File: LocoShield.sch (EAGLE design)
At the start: 15 parts, among them J2 RJ12, J3 RJ12, Q1 2N3904, U1 LM393N

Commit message: 0.1
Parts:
- LED1: device MCP:LEDB155 -> led:LEDB156
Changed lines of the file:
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@@
 <layers>
 <layer number="1" name="Top" color="4" fill="1" visible="no" active="no"/>
+<layer number="2" name="Route2" color="1" fill="3" visible="no" active="no"/>
+<layer number="3" name="Route3" color="4" fill="3" visible="no" active="no"/>
+<layer number="14" name="Route14" color="1" fill="6" visible="no" active="no"/>
+<layer number="15" name="Route15" color="4" fill="6" visible="no" active="no"/>
 <layer number="16" name="Bottom" color="2" fill="1" visible="no" active="no"/>
 <layer number="17" name="Pads" color="6" fill="1" visible="no" active="no"/>
@@
 <part name="U1" library="MCP" deviceset="LM393" device="N"/>
 <part name="R9" library="rcl" deviceset="R-US_" device="0204/5" value="47R"/>
-<part name="LED1" library="MCP" deviceset="LED" device="B155"/>
+<part name="LED1" library="led" deviceset="LED" device="B156"/>
 <part name="J1" library="con-lstb" deviceset="MA04-1" device=""/>
 <part name="P+1" library="supply1" deviceset="VCC" device=""/>

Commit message: 1.0
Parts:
- added U2: ARDUINO_SHIELDNOHOLES, SparkFun:ARDUINO_SHIELDNOHOLES
- LED1: device led:LEDB156 -> led:LEDB155
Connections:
- net GND: now also U2.GND@0, U2.GND@1, U2.GND@2
- net LNRX: now also U2.D8
- net LNTX: now also U2.D7
- net VCC: now also U2.5V
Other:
- note added: "Loconet Shield"
- note removed: "Loconet Protoboard"
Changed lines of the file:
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@@
 <layer number="18" name="Vias" color="2" fill="1" visible="no" active="no"/>
 <layer number="19" name="Unrouted" color="21" fill="1" visible="no" active="no"/>
-<layer number="20" name="Dimension" color="24" fill="1" visible="no" active="no"/>
+<layer number="20" name="Dimension" color="27" fill="1" visible="no" active="no"/>
 <layer number="21" name="tPlace" color="3" fill="1" visible="no" active="no"/>
 <layer number="22" name="bPlace" color="14" fill="1" visible="no" active="no"/>
@@
 <layer number="49" name="Reference" color="12" fill="1" visible="no" active="no"/>
 <layer number="50" name="dxf" color="7" fill="1" visible="no" active="no"/>
-<layer number="51" name="tDocu" color="6" fill="1" visible="no" active="no"/>
+<layer number="51" name="tDocu" color="61" fill="1" visible="no" active="no"/>
 <layer number="52" name="bDocu" color="7" fill="1" visible="no" active="no"/>
 <layer number="53" name="tGND_GNDA" color="7" fill="9" visible="no" active="no"/>
@@
 <layer number="121" name="_tsilk" color="7" fill="1" visible="yes" active="yes"/>
 <layer number="122" name="_bsilk" color="7" fill="1" visible="yes" active="yes"/>
+<layer number="125" name="_tNames" color="7" fill="1" visible="no" active="yes"/>
+<layer number="144" name="Drill_legend" color="7" fill="1" visible="no" active="yes"/>
 <layer number="151" name="HeatSink" color="7" fill="1" visible="yes" active="yes"/>
 <layer number="199" name="Contour" color="7" fill="1" visible="yes" active="yes"/>
@@
 <layer number="207" name="207bmp" color="8" fill="10" visible="yes" active="yes"/>
 <layer number="208" name="208bmp" color="9" fill="10" visible="yes" active="yes"/>
+<layer number="209" name="209bmp" color="7" fill="1" visible="no" active="yes"/>
+<layer number="210" name="210bmp" color="7" fill="1" visible="no" active="yes"/>
+<layer number="211" name="211bmp" color="7" fill="1" visible="no" active="yes"/>
+<layer number="212" name="212bmp" color="7" fill="1" visible="no" active="yes"/>
+<layer number="213" name="213bmp" color="7" fill="1" visible="no" active="yes"/>
+<layer number="214" name="214bmp" color="7" fill="1" visible="no" active="yes"/>
+<layer number="215" name="215bmp" color="7" fill="1" visible="no" active="yes"/>
+<layer number="216" name="216bmp" color="7" fill="1" visible="no" active="yes"/>
+<layer number="217" name="217bmp" color="18" fill="1" visible="no" active="no"/>
+<layer number="218" name="218bmp" color="19" fill="1" visible="no" active="no"/>
+<layer number="219" name="219bmp" color="20" fill="1" visible="no" active="no"/>
+<layer number="220" name="220bmp" color="21" fill="1" visible="no" active="no"/>
+<layer number="221" name="221bmp" color="22" fill="1" visible="no" active="no"/>
+<layer number="222" name="222bmp" color="23" fill="1" visible="no" active="no"/>
+<layer number="223" name="223bmp" color="24" fill="1" visible="no" active="no"/>
+<layer number="224" name="224bmp" color="25" fill="1" visible="no" active="no"/>
 <layer number="250" name="Descript" color="3" fill="1" visible="yes" active="yes"/>
 <layer number="251" name="SMDround" color="12" fill="11" visible="yes" active="yes"/>
@@
 <part name="U1" library="MCP" deviceset="LM393" device="N"/>
 <part name="R9" library="rcl" deviceset="R-US_" device="0204/5" value="47R"/>
-<part name="LED1" library="led" deviceset="LED" device="B156"/>
+<part name="LED1" library="led" deviceset="LED" device="B155"/>
 <part name="J1" library="con-lstb" deviceset="MA04-1" device=""/>
 <part name="P+1" library="supply1" deviceset="VCC" device=""/>
 <part name="V3" library="supply2" deviceset="GND" device=""/>
+<part name="U2" library="SparkFun" deviceset="ARDUINO_SHIELD" device="NOHOLES"/>
+<part name="P+2" library="supply1" deviceset="VCC" device=""/>
+<part name="V4" library="supply2" deviceset="GND" device=""/>
 </parts>
 <sheets>
@@
 <wire x1="70.612" y1="62.23" x2="70.612" y2="137.16" width="0.1524" layer="250"/>
 <text x="105.41" y="68.58" size="2.54" layer="250">Loconet Interface</text>
-<text x="154.94" y="27.94" size="5.08" layer="250">Loconet Protoboard</text>
+<text x="154.94" y="27.94" size="5.08" layer="250">Loconet Shield</text>
 <text x="238.76" y="7.62" size="2.54" layer="250">1.0</text>
 <text x="195.58" y="96.52" size="1.778" layer="92">D7</text>
@@
 <instance part="P+1" gate="VCC" x="185.42" y="104.14"/>
 <instance part="V3" gate="GND" x="185.42" y="91.44"/>
+<instance part="U2" gate="G$1" x="205.74" y="152.4"/>
+<instance part="P+2" gate="VCC" x="187.96" y="149.86"/>
+<instance part="V4" gate="GND" x="187.96" y="132.08"/>
 </instances>
 <busses>
@@
 <pinref part="V3" gate="GND" pin="GND"/>
 </segment>
+<segment>
+<wire x1="193.04" y1="139.7" x2="193.04" y2="137.16" width="0.1524" layer="91"/>
+<wire x1="193.04" y1="137.16" x2="193.04" y2="134.62" width="0.1524" layer="91"/>
+<wire x1="193.04" y1="134.62" x2="187.96" y2="134.62" width="0.1524" layer="91"/>
+<junction x="193.04" y="137.16"/>
+<junction x="193.04" y="134.62"/>
+<pinref part="U2" gate="G$1" pin="GND@2"/>
+<pinref part="U2" gate="G$1" pin="GND@1"/>
+<pinref part="U2" gate="G$1" pin="GND@0"/>
+<pinref part="V4" gate="GND" pin="GND"/>
+</segment>
 </net>
 <net name="DCCRAILSYNC-" class="0">
@@
 <pinref part="J1" gate="1" pin="1"/>
 <pinref part="P+1" gate="VCC" pin="VCC"/>
+</segment>
+<segment>
+<wire x1="193.04" y1="147.32" x2="187.96" y2="147.32" width="0.1524" layer="91"/>
+<pinref part="U2" gate="G$1" pin="5V"/>
+<pinref part="P+2" gate="VCC" pin="VCC"/>
 </segment>
 </net>
@@
 <pinref part="R1" gate="G$1" pin="1"/>
 </segment>
+<segment>
+<wire x1="218.44" y1="149.86" x2="223.52" y2="149.86" width="0.1524" layer="91"/>
+<label x="223.52" y="149.86" size="1.016" layer="95" xref="yes"/>
+<pinref part="U2" gate="G$1" pin="D7"/>
+</segment>
 </net>
 <net name="LNRX" class="0">
@@
 <pinref part="LED1" gate="G$1" pin="C"/>
 </segment>
-</net>
+<segment>
+<wire x1="218.44" y1="147.32" x2="223.52" y2="147.32" width="0.1524" layer="91"/>
+<label x="223.52" y="147.32" size="1.016" layer="95" xref="yes"/>
+<pinref part="U2" gate="G$1" pin="D8"/>
+</segment>
+</net>

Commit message: 1.1
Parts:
- removed J1: (no value), con-lstb:MA04-1
- added JP1, JP2, JP5, JP6: (no value), MCP:JUMPER-2PTH_LOCK
- added JP3: LN-TERM, MCP:JUMPER-2PTH_LOCK
- added JP4: (no value), MCP:M05LOCK
- added R10: 82R, rcl:R-US_0204/5
- added SHIELD: ARDUINO_SHIELDNOHOLES, SparkFun:ARDUINO_SHIELDNOHOLES
- U1: value LM393N -> LM393; device MCP:LM393N -> MCP:LM393
- U2: value ARDUINO_SHIELDNOHOLES -> LM317LZ; device SparkFun:ARDUINO_SHIELDNOHOLES -> linear:LM317LZ
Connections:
- new net N$10: JP6.1, SHIELD.D4
- new net N$3: JP1.1, SHIELD.D7
- new net N$4: JP2.1, SHIELD.D8
- new net N$7: R10.1, U2.VO
- new net N$8: JP3.2, R10.2, U2.ADJ
- new net N$9: JP5.1, SHIELD.*D5
- new net V+: JP4.1, SHIELD.VIN, U2.VI
- net GND: now also JP4.5, SHIELD.GND@0, SHIELD.GND@1, SHIELD.GND@2; no longer J1.4, U2.GND@0, U2.GND@1, U2.GND@2
- net LNRX: now also JP2.2, JP4.3, JP6.2; no longer J1.2, U2.D8
- net LNTX: now also JP1.2, JP4.4, JP5.2; no longer J1.3, U2.D7
- net LOCONET: now also JP3.1
- net VCC: now also JP4.2, SHIELD.5V; no longer J1.1, U2.5V
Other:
- note added: "1.1C"
- note added: "LocoShield"
- note removed: "1.0"
- note removed: "Loconet Shield"

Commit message: 1.2
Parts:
- removed JP3: LN-TERM, MCP:JUMPER-2PTH_LOCK
- removed JP4: (no value), MCP:M05LOCK
- removed JP5, JP6: (no value), MCP:JUMPER-2PTH_LOCK
- removed R10: 82R, rcl:R-US_0204/5
- removed SHIELD: ARDUINO_SHIELDNOHOLES, SparkFun:ARDUINO_SHIELDNOHOLES
- added J1: (no value), con-lstb:MA04-1
- LED1: device led:LEDB155 -> MCP:LEDCHIPLED_0805
- Q1: device transistor:2N3904 -> MCP:NPN-SOT23-3
- R1: value 4k7 -> 470R; device rcl:R-US_0204/5 -> rcl:R-US_R0805W
- R2: value 27k -> 1k; device rcl:R-US_0204/5 -> rcl:R-US_R0805W
- R3: value 39k -> 27k; device rcl:R-US_0204/5 -> rcl:R-US_R0805W
- R4: value 47k -> 39k; device rcl:R-US_0204/5 -> rcl:R-US_R0805W
- R5: value 150k -> 240k; device rcl:R-US_0204/5 -> rcl:R-US_R0805W
- R6: value 240k -> 150k; device rcl:R-US_0204/5 -> rcl:R-US_R0805W
- R7: value 1k -> 47k; device rcl:R-US_0204/5 -> rcl:R-US_R0805W
- R8: value 470R -> 47R; device rcl:R-US_0204/5 -> rcl:R-US_R0805W
- R9: value 47R -> 4k7; device rcl:R-US_0204/5 -> rcl:R-US_R0805W
- U1: value LM393 -> LM393M; device MCP:LM393 -> MCP:LM393M
- U2: value LM317LZ -> ARDUINO_SHIELDNOHOLES; device linear:LM317LZ -> SparkFun:ARDUINO_SHIELDNOHOLES
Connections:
- removed net N$10: JP6.1, SHIELD.D4
- removed net N$7: R10.1, U2.VO
- removed net N$8: JP3.2, R10.2, U2.ADJ
- removed net N$9: JP5.1, SHIELD.*D5
- removed net V+: JP4.1, SHIELD.VIN, U2.VI
- net GND: now also J1.4, R4.1, R6.1, R8.1, U2.GND@0, U2.GND@1, U2.GND@2; no longer JP4.5, R3.1, R5.1, R9.1, SHIELD.GND@0, SHIELD.GND@1, SHIELD.GND@2
- net LNRX: now also J1.2, R2.2, R5.2; no longer JP4.3, JP6.2, R6.2, R7.2
- net LNTX: now also J1.3, R9.1; no longer JP4.4, JP5.2, R1.1
- net LOCONET: now also R7.1; no longer JP3.1, R4.1
- net N$1: now also R9.2; no longer R1.2
- net N$15: now also R1.2; no longer R8.2
- net N$2: now also R5.1, R6.2, R7.2; no longer R4.2, R5.2, R6.1
- net N$3: now also U2.D7; no longer SHIELD.D7
- net N$4: now also U2.D8; no longer SHIELD.D8
- net N$5: now also R4.2; no longer R2.2
- net N$6: now also R8.2; no longer R9.2
- net VCC: now also J1.1, R1.1, R3.1, U2.5V; no longer JP4.2, R7.1, R8.1, SHIELD.5V
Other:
- note added: "1.2"
- note added: "Loconet Shield"
- note removed: "1.1C"
- note removed: "LocoShield"
- moved on the sheet: R1, R2, R3, R4, R5, R6, R7, R8, R9

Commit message: 1.3
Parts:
- removed J1: (no value), con-lstb:MA04-1
- added JP3: LN-TERM, MCP:JUMPER-2PTH_LOCK
- added R10: 82R, rcl:R-US_R0805
- added SHIELD: ARDUINO_SHIELDNOHOLES, SparkFun:ARDUINO_SHIELDNOHOLES
- added SV1: (no value), con-lstb:MA05-1
- U2: value ARDUINO_SHIELDNOHOLES -> LM317LCDR; device SparkFun:ARDUINO_SHIELDNOHOLES -> MCP:LM317LD
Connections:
- new net N$20: JP3.2, R10.2, U2.ADJ
- new net V+: SHIELD.VIN, SV1.1, U2.VI
- new net VOUT: R10.1, U2.VO, U2.VO@1, U2.VO@2, U2.VO@3
- net GND: now also SHIELD.GND@0, SHIELD.GND@1, SHIELD.GND@2, SV1.5; no longer J1.4, U2.GND@0, U2.GND@1, U2.GND@2
- net LNRX: now also SV1.3; no longer J1.2
- net LNTX: now also SV1.4; no longer J1.3
- net LOCONET: now also JP3.1
- net N$3: now also SHIELD.D7; no longer U2.D7
- net N$4: now also SHIELD.D8; no longer U2.D8
- net VCC: now also SHIELD.5V, SV1.2; no longer J1.1, U2.5V
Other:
- note added: "1.3"
- note removed: "1.2"

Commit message: 1.4
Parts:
- removed JP1, JP2: (no value), MCP:JUMPER-2PTH_LOCK
- added JPD10, JPD11, JPD4, JPD5, JPD6, JPD7, JPD8, JPD9: (no value), MCP:JP2E
- LED1: value (none) -> Blue; device MCP:LEDCHIPLED_0805 -> SPCoast:LED0805-LED
- R1, R2, R3, R4, R5, R6, R7, R8, R9: device rcl:R-US_R0805W -> SPCoast:R0805-RES
- R10: device rcl:R-US_R0805 -> SPCoast:R0805-RES
- SHIELD: value ARDUINO_SHIELDNOHOLES -> ARDUINO_SHIELDNO_SILK; device SparkFun:ARDUINO_SHIELDNOHOLES -> SPCoast:ARDUINO_SHIELDNO_SILK
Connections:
- removed net N$3: JP1.1, SHIELD.D7
- removed net N$4: JP2.1, SHIELD.D8
- new net D10: JPD10.2, SHIELD.*D10
- new net D11: JPD11.2, SHIELD.*D11
- new net D4: JPD4.2, SHIELD.D4
- new net D5: JPD5.2, SHIELD.*D5
- new net D6: JPD6.2, SHIELD.*D6
- new net D7: JPD7.2, SHIELD.D7
- new net D8: JPD8.2, SHIELD.D8
- new net D9: JPD9.2, SHIELD.*D9
- net GND: now also R8.2; no longer R8.1
- net LNRX: now also JPD10.1, JPD11.1, JPD4.1, JPD5.1, JPD6.1, JPD7.1, JPD8.1, JPD9.1; no longer JP2.2
- net LNTX: now also JPD10.3, JPD11.3, JPD4.3, JPD5.3, JPD6.3, JPD7.3, JPD8.3, JPD9.3; no longer JP1.2
- net N$6: now also R8.1; no longer R8.2
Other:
- note added: "1.4"
- note added: "Added D4-D11 RX/TX selection jumpers"
- note removed: "1.3"
- moved on the sheet: J2, J3, JP3, Q1, SV1, U1G1, U1G2, U2

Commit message: added missing values
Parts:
- J2, J3: value RJ12 -> RJ12/6
- JPD10, JPD11, JPD4, JPD5, JPD6, JPD7, JPD8, JPD9, SV1: value (none) -> 0.100
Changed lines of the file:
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@@
 </classes>
 <parts>
-<part name="J2" library="con-amp" deviceset="520250-3" device="" value="RJ12"/>
-<part name="J3" library="con-amp" deviceset="520250-3" device="" value="RJ12"/>
+<part name="J2" library="con-amp" deviceset="520250-3" device="" value="RJ12/6"/>
+<part name="J3" library="con-amp" deviceset="520250-3" device="" value="RJ12/6"/>
 <part name="V1" library="supply2" deviceset="GND" device=""/>
 <part name="R9" library="SPCoast" deviceset="R*" device="0805-RES" value="4k7"/>
@@
 <part name="U2" library="MCP" deviceset="LM317LD" device="" value="LM317LCDR"/>
 <part name="P+3" library="supply1" deviceset="V+" device=""/>
-<part name="SV1" library="con-lstb" deviceset="MA05-1" device=""/>
+<part name="SV1" library="con-lstb" deviceset="MA05-1" device="" value="0.100"/>
 <part name="P+4" library="supply1" deviceset="V+" device=""/>
-<part name="JPD7" library="MCP" deviceset="JP2E" device=""/>
-<part name="JPD6" library="MCP" deviceset="JP2E" device=""/>
-<part name="JPD5" library="MCP" deviceset="JP2E" device=""/>
-<part name="JPD4" library="MCP" deviceset="JP2E" device=""/>
-<part name="JPD8" library="MCP" deviceset="JP2E" device=""/>
-<part name="JPD9" library="MCP" deviceset="JP2E" device=""/>
-<part name="JPD10" library="MCP" deviceset="JP2E" device=""/>
-<part name="JPD11" library="MCP" deviceset="JP2E" device=""/>
+<part name="JPD7" library="MCP" deviceset="JP2E" device="" value="0.100"/>
+<part name="JPD6" library="MCP" deviceset="JP2E" device="" value="0.100"/>
+<part name="JPD5" library="MCP" deviceset="JP2E" device="" value="0.100"/>
+<part name="JPD4" library="MCP" deviceset="JP2E" device="" value="0.100"/>
+<part name="JPD8" library="MCP" deviceset="JP2E" device="" value="0.100"/>
+<part name="JPD9" library="MCP" deviceset="JP2E" device="" value="0.100"/>
+<part name="JPD10" library="MCP" deviceset="JP2E" device="" value="0.100"/>
+<part name="JPD11" library="MCP" deviceset="JP2E" device="" value="0.100"/>
 </parts>
 <sheets>

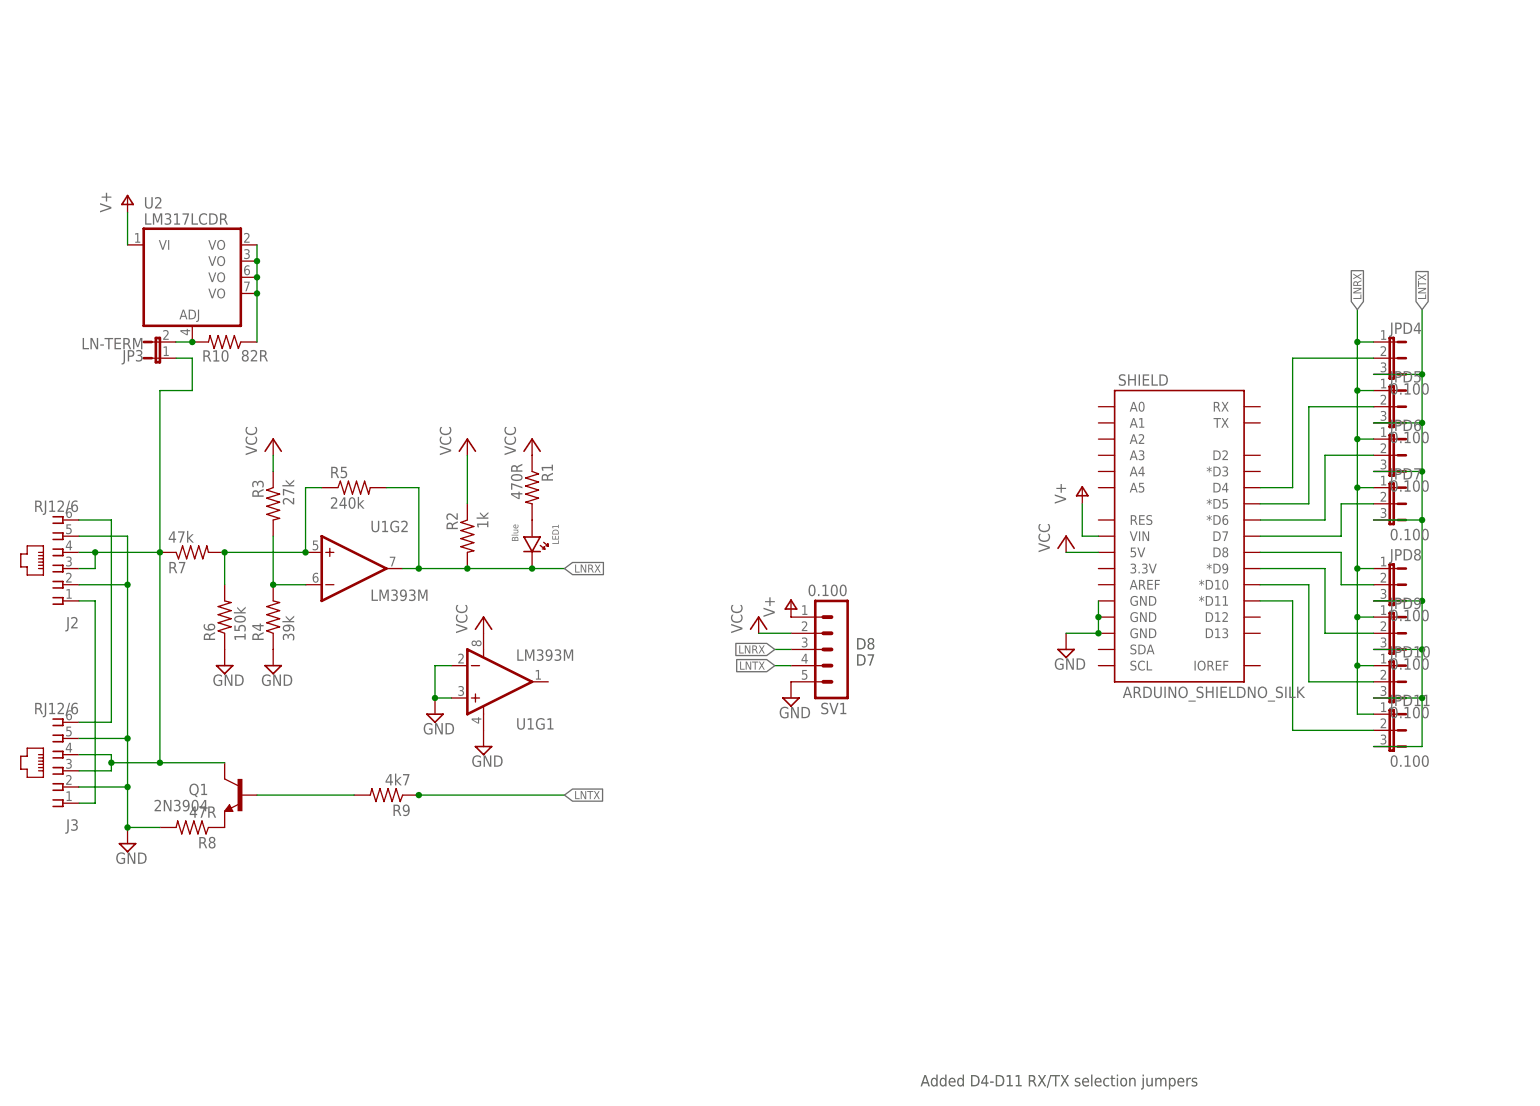
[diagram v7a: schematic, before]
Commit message: normalized values
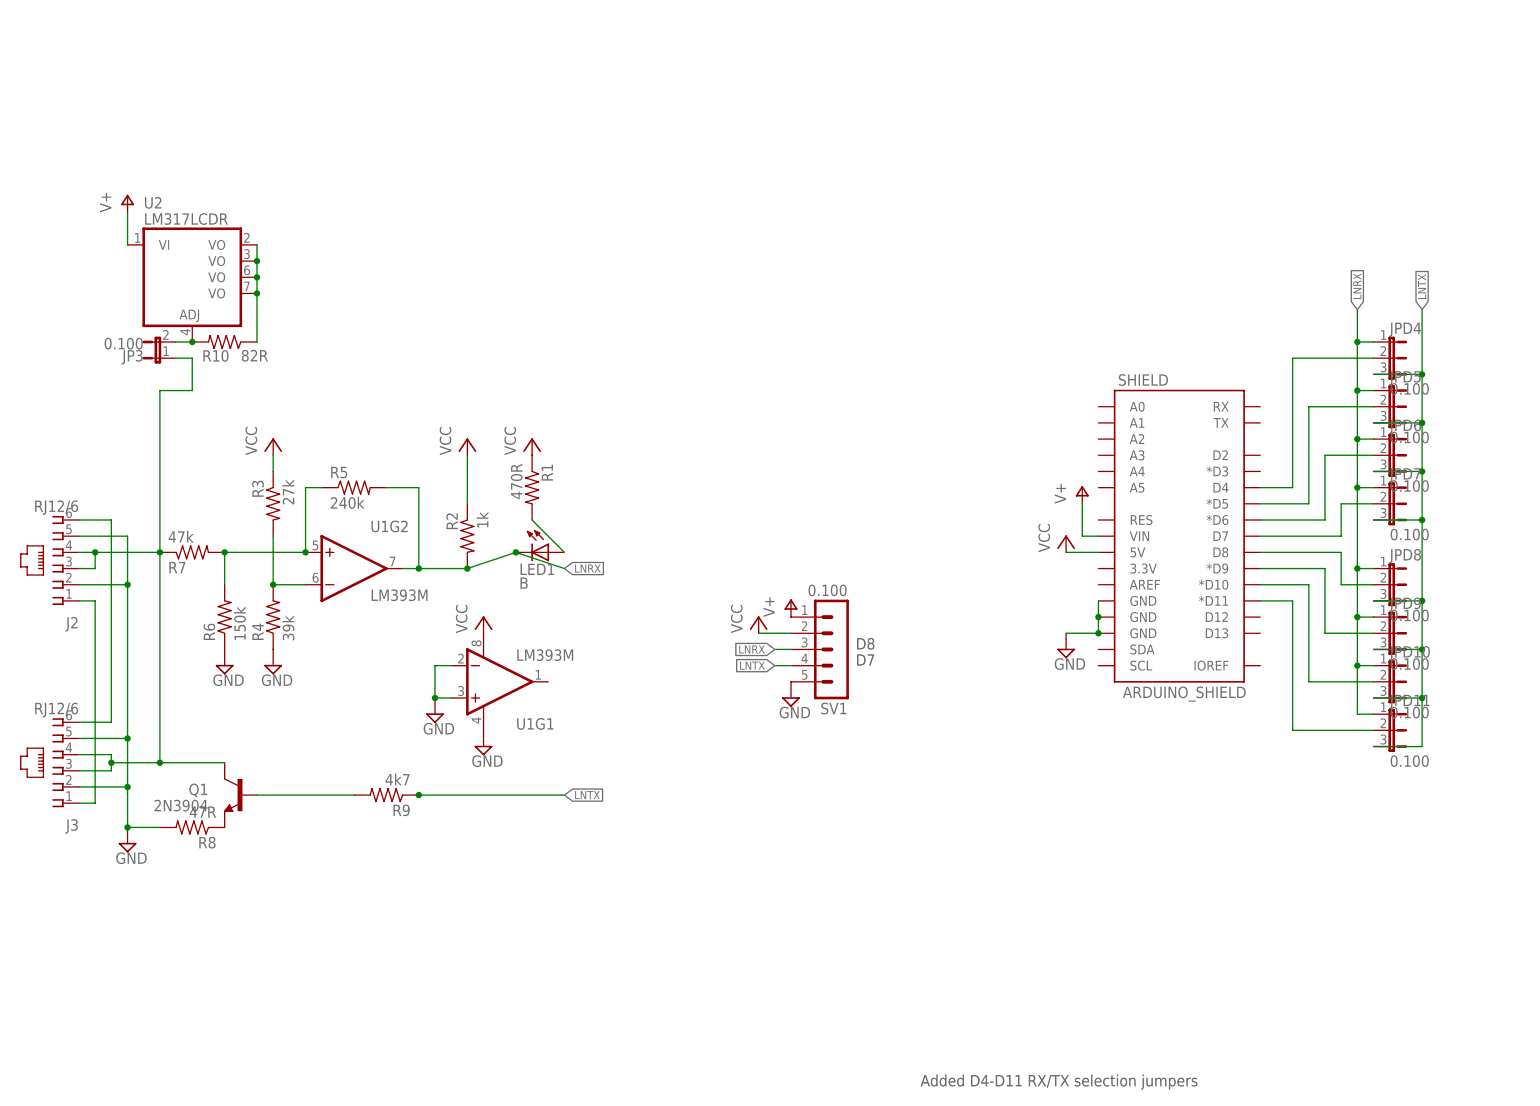
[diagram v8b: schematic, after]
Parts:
- J2, J3: device con-amp:520250-3 -> SPCoast:CONNECTOR-RJ25-6P6C
- JP3: value LN-TERM -> 0.100
- LED1: value Blue -> B; device SPCoast:LED0805-LED -> SPCoast:LED0603-LED
- R1, R2, R3, R4, R5, R6, R7, R8, R9: device SPCoast:R0805-RES -> SPCoast:R0603-RES
- SHIELD: value ARDUINO_SHIELDNO_SILK -> ARDUINO_SHIELD
